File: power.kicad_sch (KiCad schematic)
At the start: 25 parts, among them Q2 S8550, Q3 S8550, U1 B0505S-1WR2, U22 TLV76733DRVx, U6 LMR14006

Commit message: x
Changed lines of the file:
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@@
 	(text_box "base resistor?"
 		(exclude_from_sim no)
-		(at 41.91 92.71 0)
+		(at 43.18 85.09 0)
 		(size 52.07 19.05)
 		(stroke

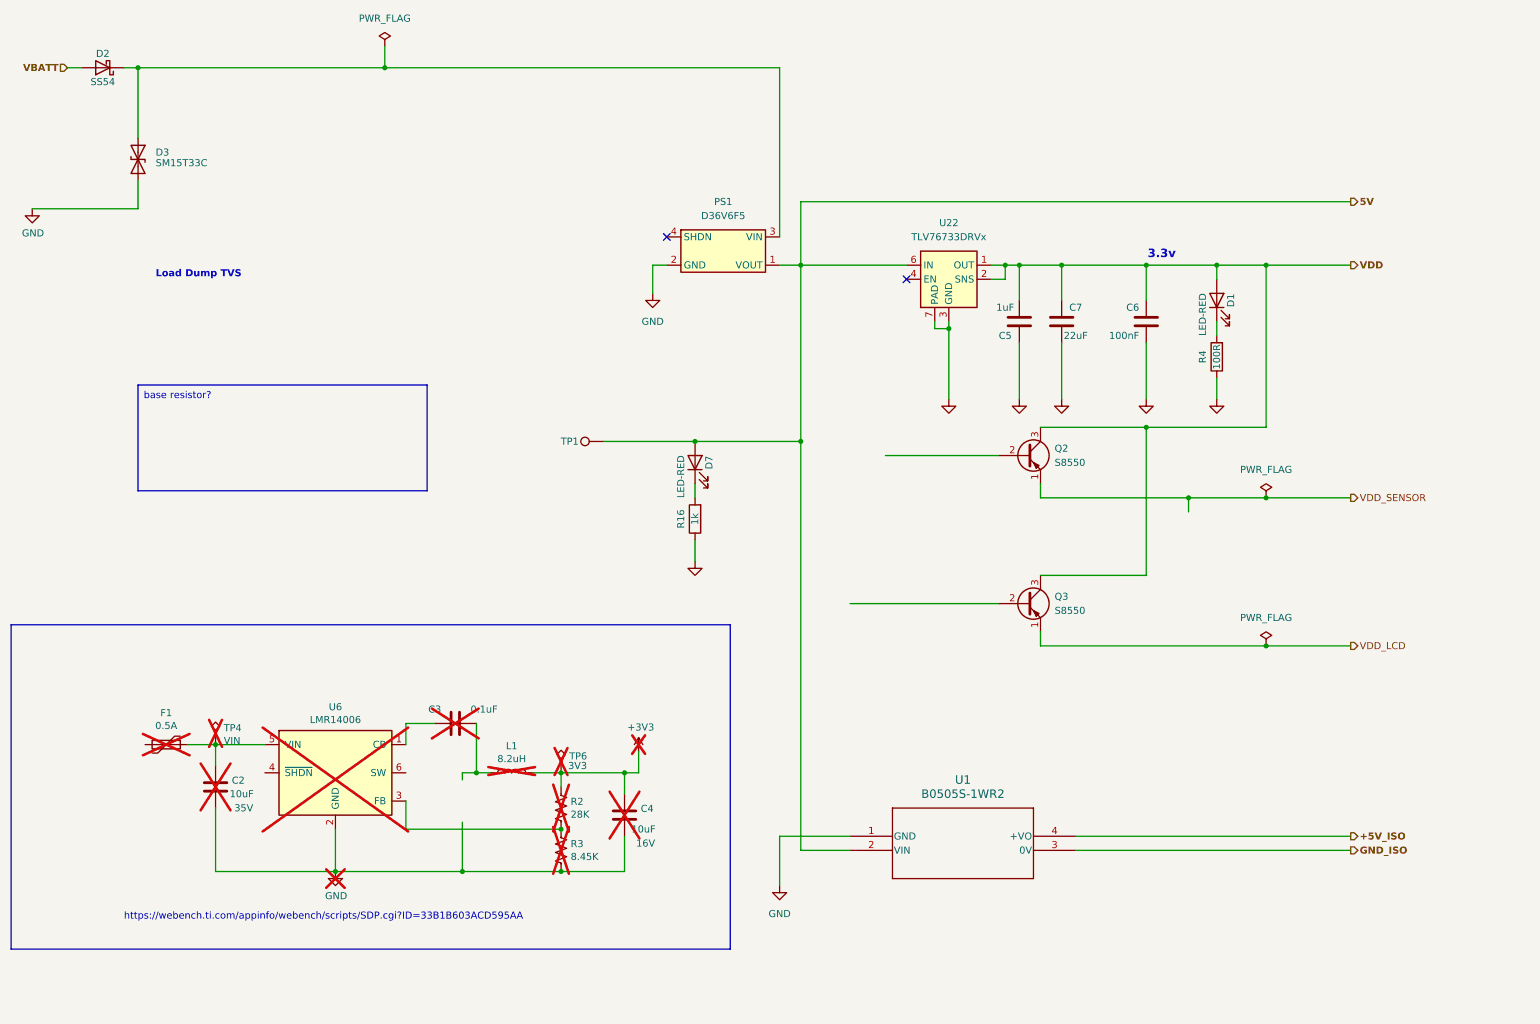
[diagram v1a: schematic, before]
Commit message: change power add buzzer
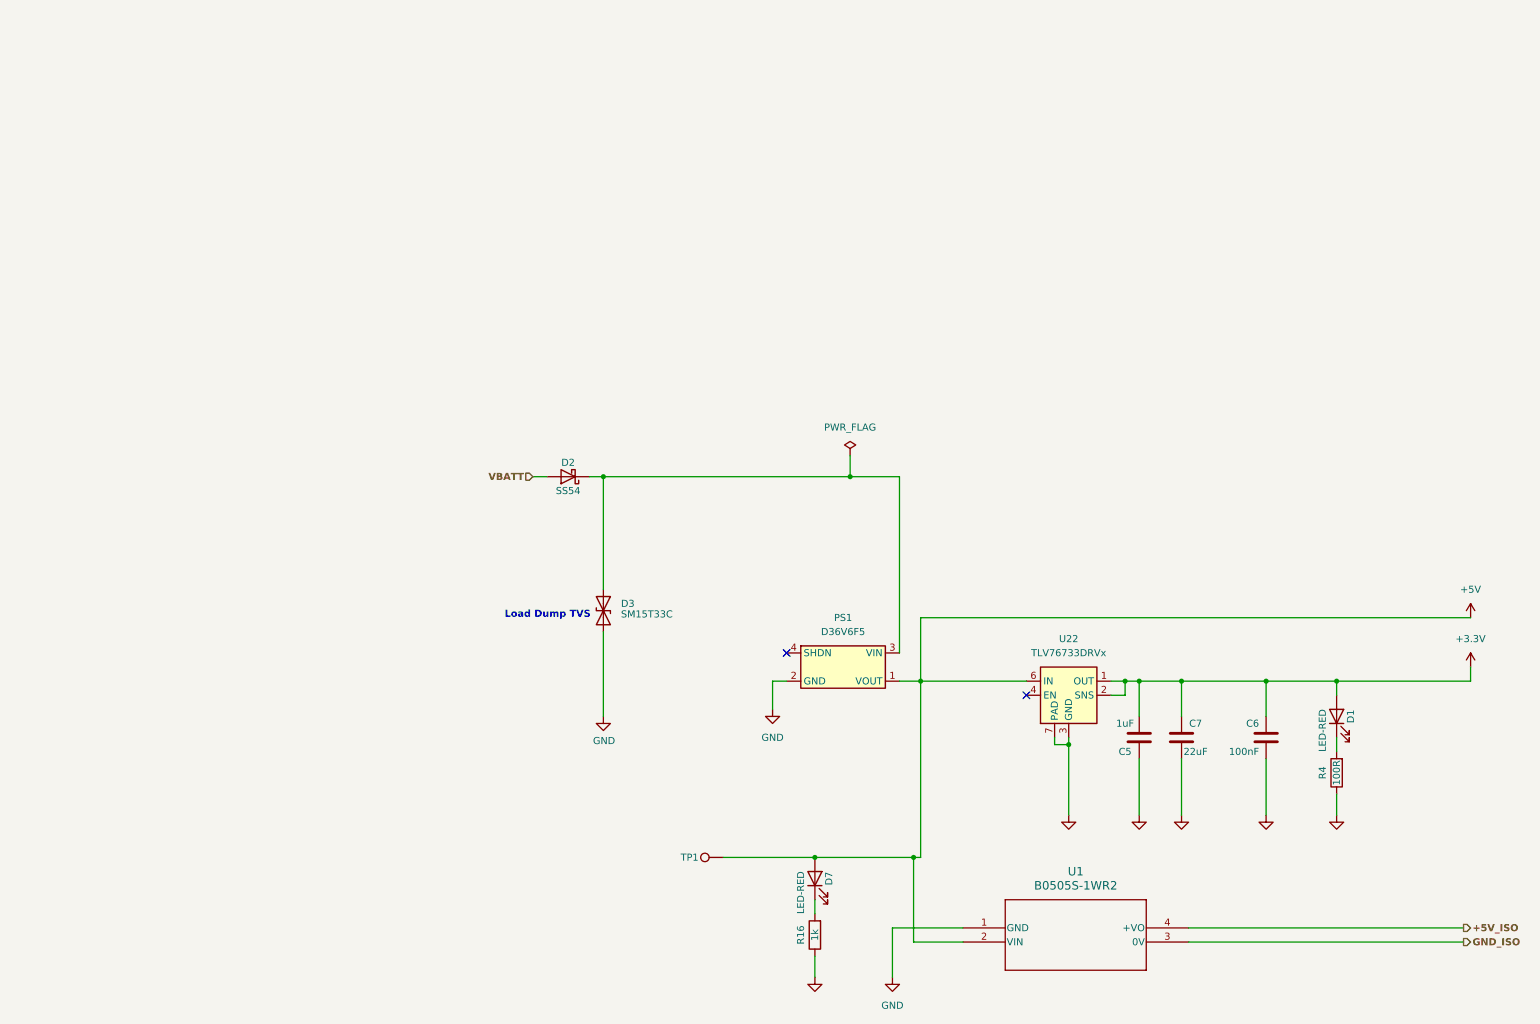
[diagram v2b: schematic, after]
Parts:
- removed C2, C4: 10uF, Capacitor_SMD:C_1206_3216Metric, symbol Device:C
- removed C3: 0.1uF, Capacitor_SMD:C_0603_1608Metric, symbol Device:C
- removed F1: 0.5A, Fuse:Fuse_1812_4532Metric, symbol Device:Polyfuse
- removed L1: 8.2uH, voltlog:Inductor_7.5x6.6, symbol Device:L
- removed Q2, Q3: S8550, Package_TO_SOT_SMD:SOT-23, symbol Transistor_BJT:S8550
- removed R2: 28K, Resistor_SMD:R_0603_1608Metric, symbol Device:R_US
- removed R3: 8.45K, Resistor_SMD:R_0603_1608Metric, symbol Device:R_US
- removed TP4: VIN, TestPoint:TestPoint_Pad_D1.0mm, symbol Connector:TestPoint_Alt
- removed TP6: 3V3, TestPoint:TestPoint_Pad_D1.0mm, symbol Connector:TestPoint_Alt
- removed U6: LMR14006, Package_TO_SOT_SMD:SOT-23-6, symbol Regulator_Switching:LMR16006YQ
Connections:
- net 5V renamed +5V
- net VDD renamed +3.3V
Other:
- note removed: "3.3v"
- note removed: "https://webench.ti.com/appinfo/webench/scripts/SDP.cgi?ID=33B1B603ACD595AA"
- moved on the sheet: C5, C6, C7, D1, D2, D3, D7, PS1, R16, R4, TP1, U1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

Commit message: pre quilter
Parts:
- added TP2: +3.3V, TestPoint:TestPoint_Pad_D2.0mm, symbol Connector:TestPoint
- added TP6: 5V ISO, TestPoint:TestPoint_Pad_D2.0mm, symbol Connector:TestPoint
- added TP7: GND ISO, TestPoint:TestPoint_Pad_D2.0mm, symbol Connector:TestPoint
- U1: footprint B0505S-1WR2_MNS -> dnt:B0505S-1WR2_MNS
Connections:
- net +3.3V: now also TP2.1
- net +5V_ISO: now also TP6.1
- net GND_ISO: now also TP7.1

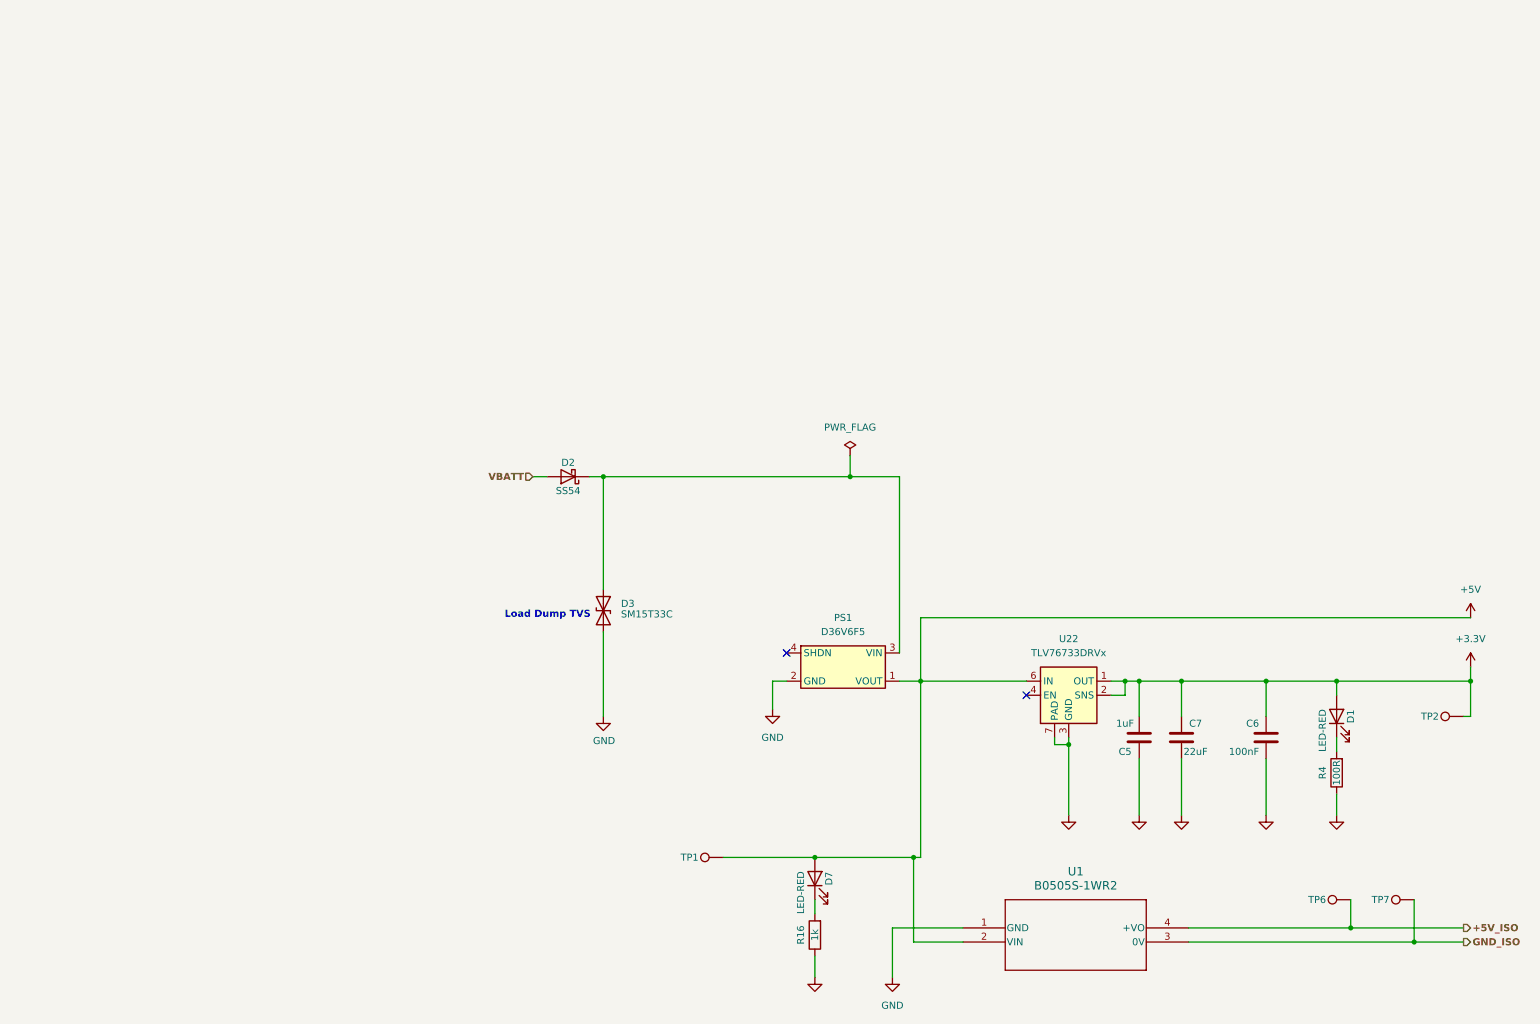
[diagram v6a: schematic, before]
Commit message: changed to tp and subbed to quilter
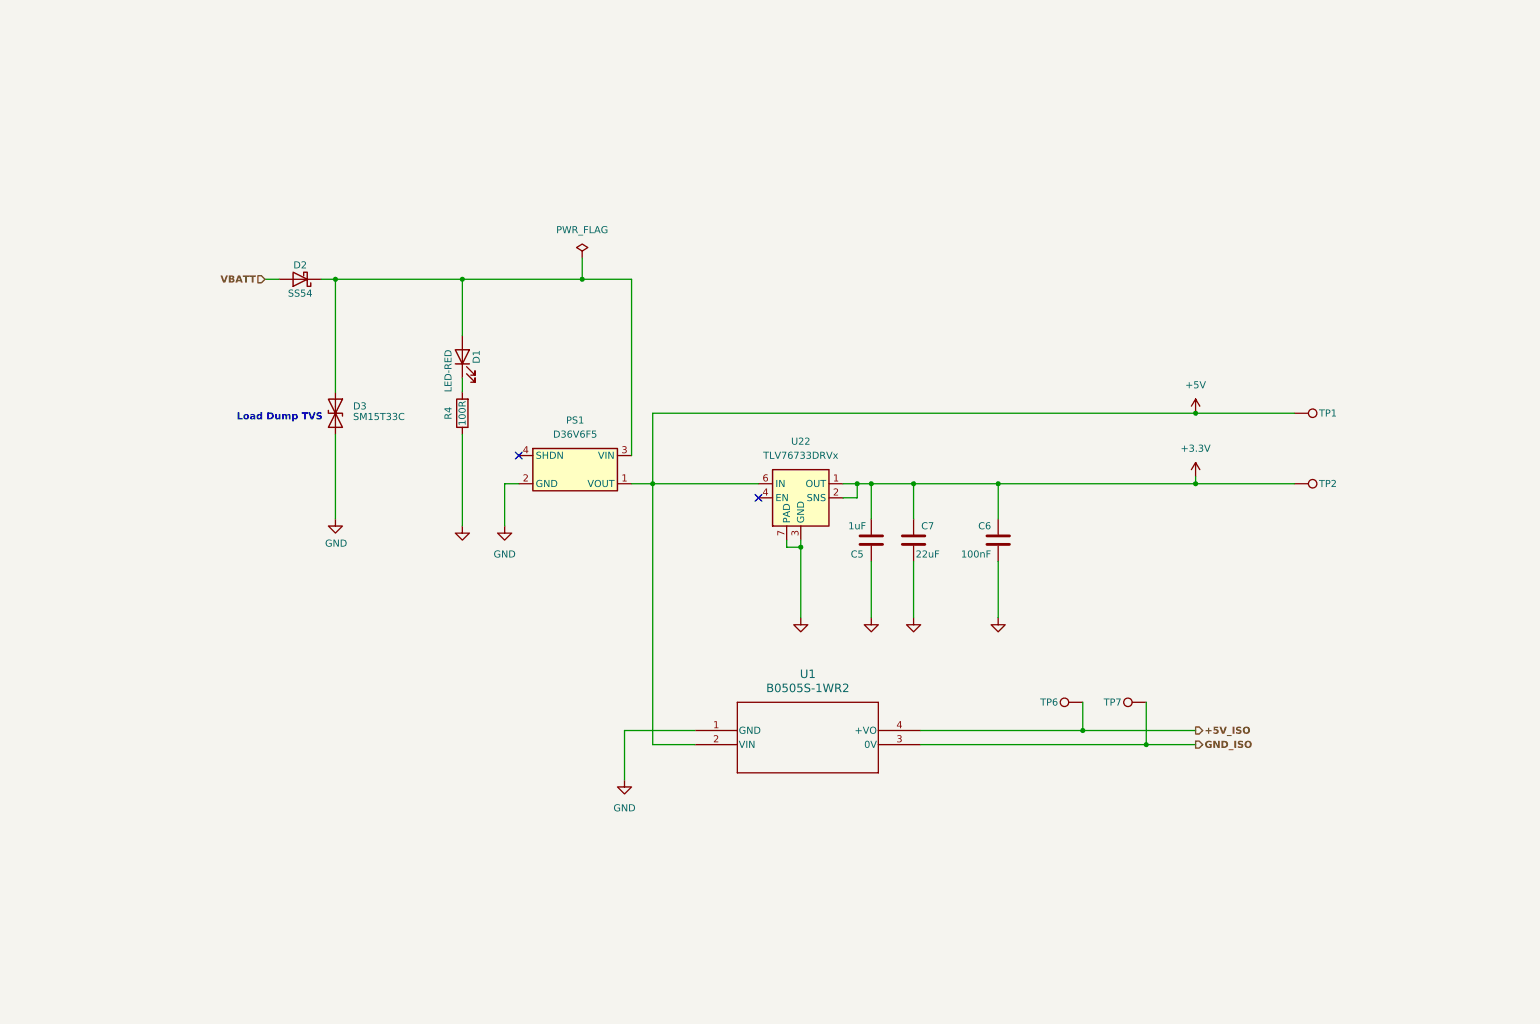
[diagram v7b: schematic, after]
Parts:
- removed D7: LED-RED, LED_SMD:LED_0603_1608Metric, symbol Device:LED
- removed R16: 1k, Resistor_SMD:R_0603_1608Metric, symbol Device:R
- TP1, TP2, TP6, TP7: footprint TestPoint:TestPoint_Pad_D2.0mm -> TestPoint:TestPoint_Pad_D1.0mm
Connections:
- net +3.3V: no longer D1.2 (A)
- net at D2.1 (K), D3.1 (A1), PS1.3 (VIN): now also D1.2 (A)
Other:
- moved on the sheet: C5, C6, C7, D2, D3, PS1, TP1, TP2, TP6, TP7, U1, U22
